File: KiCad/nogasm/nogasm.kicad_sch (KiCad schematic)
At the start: 34 parts, among them J1 Barrel_Jack, J2 AudioJack4, J3 USB_B_Micro, Q1 AP55N03K, Q2 UMH3N, SW1 SW_Push, SW2 Rotary_Encoder_Switch, SW3 SW_DIP_x04, SW4 SW_DIP_x01, U1 MPXV5100DP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

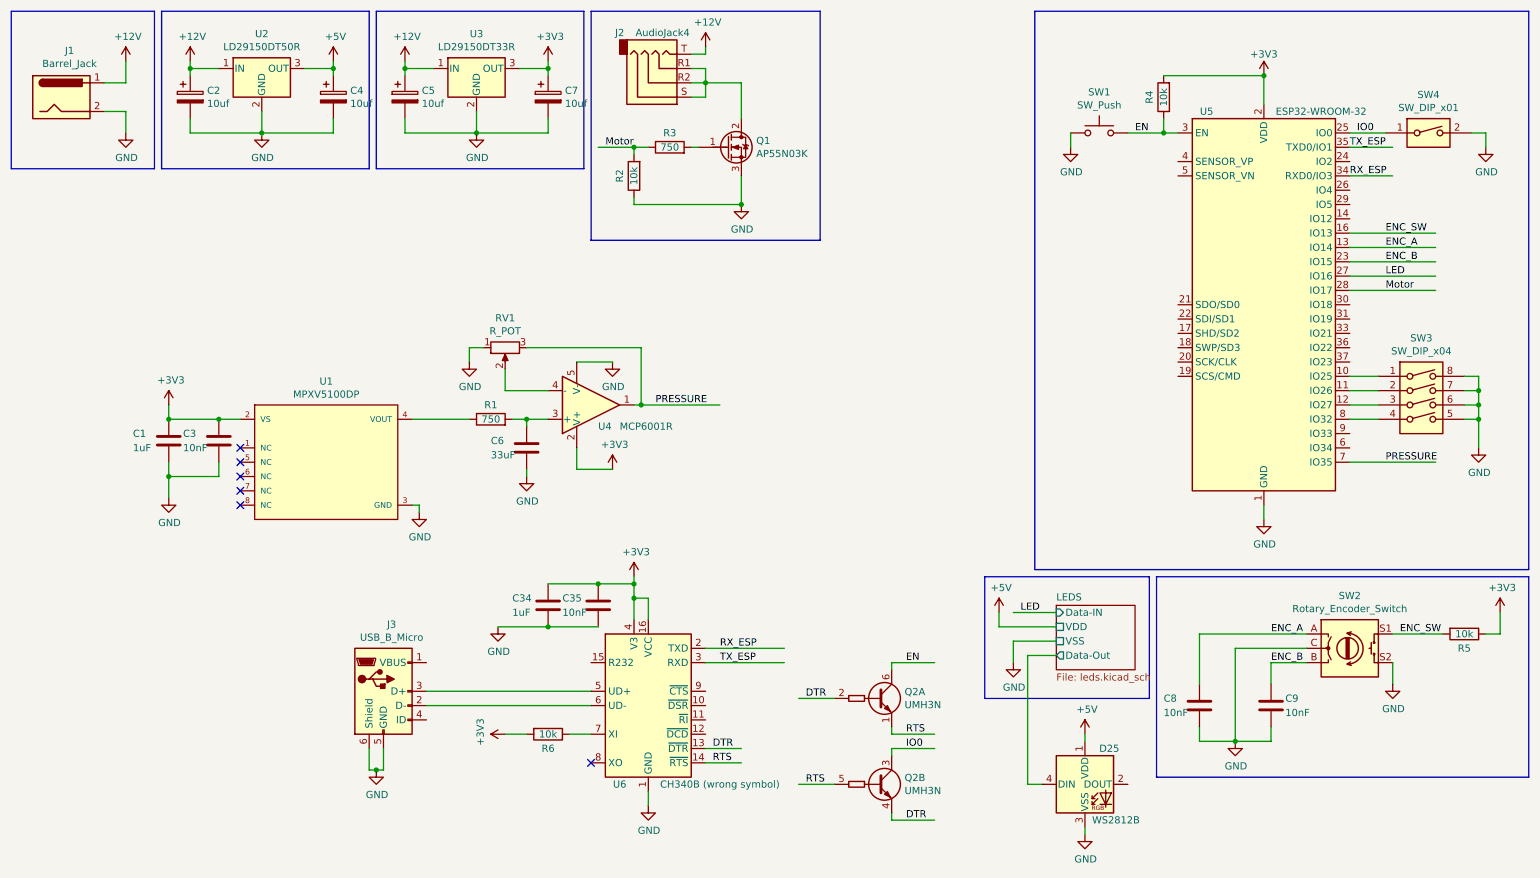
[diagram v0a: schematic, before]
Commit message: updated parts for jlc
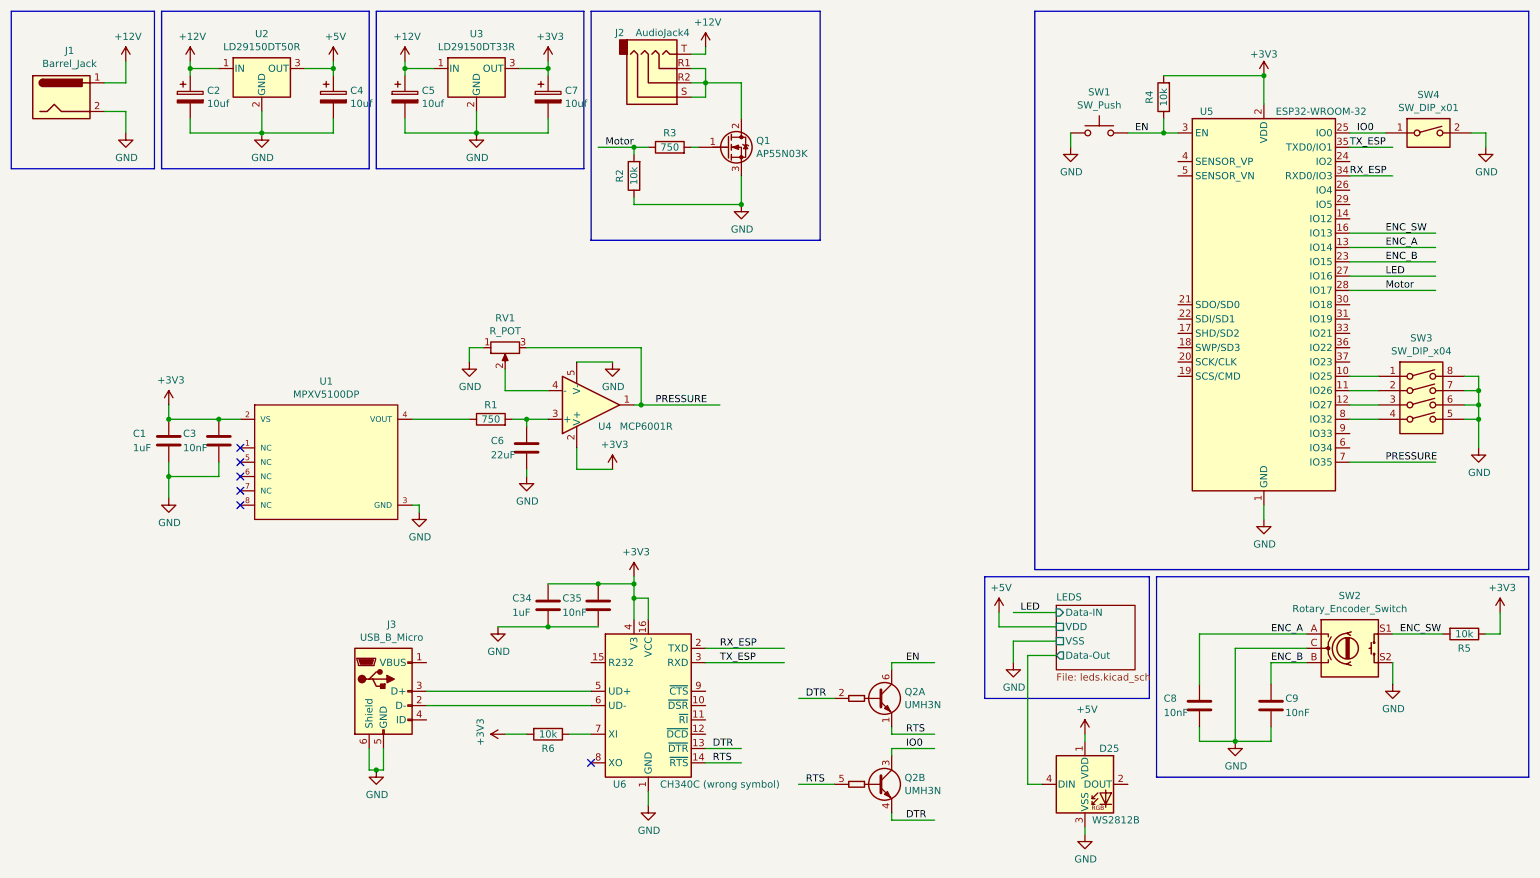
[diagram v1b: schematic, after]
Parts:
- C6: value 33uF -> 22uF; LCSC C342633 -> C159759
- Q2: LCSC (none) -> C62892
- U6: value CH340B (wrong symbol) -> CH340C (wrong symbol); LCSC C81010 -> C7464026
